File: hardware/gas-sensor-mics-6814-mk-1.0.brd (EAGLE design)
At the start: 25.4 x 22.9 mm, 7 parts, among them U1 MICS-6814

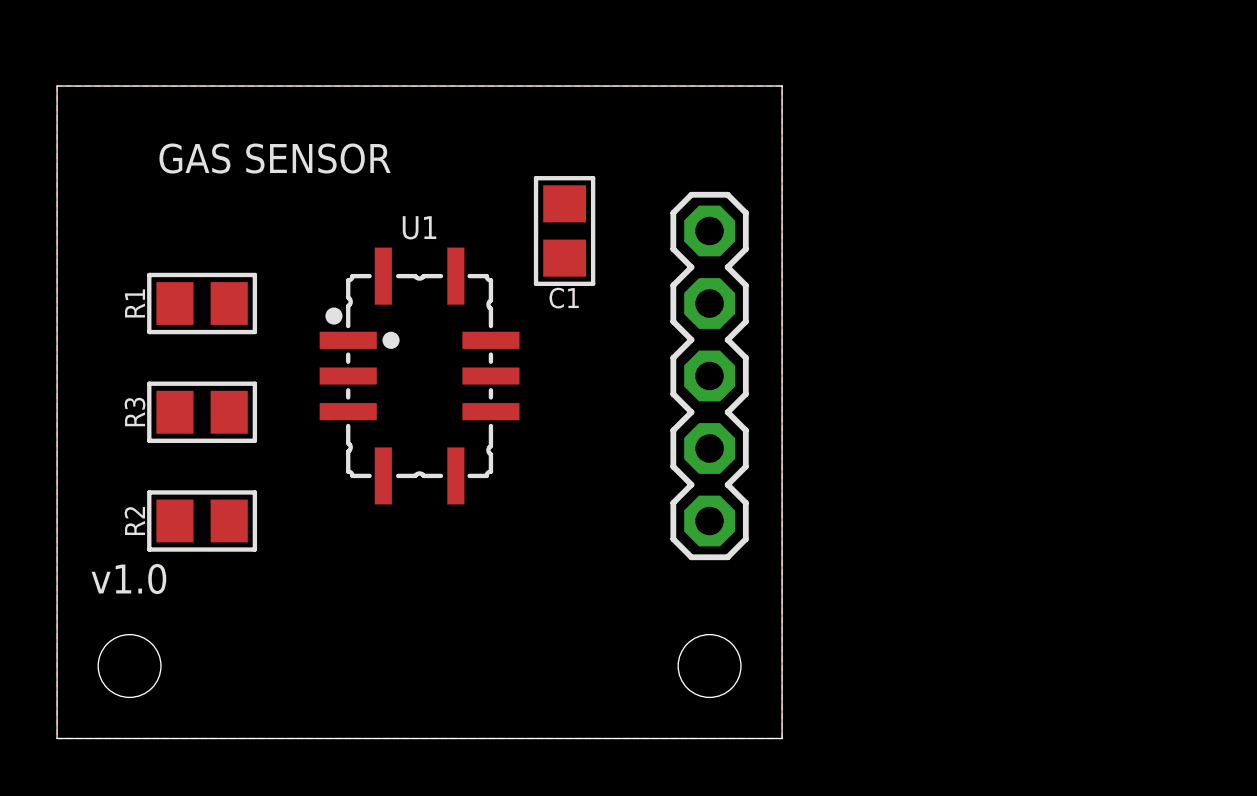
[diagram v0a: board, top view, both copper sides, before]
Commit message: gas sensor test boards
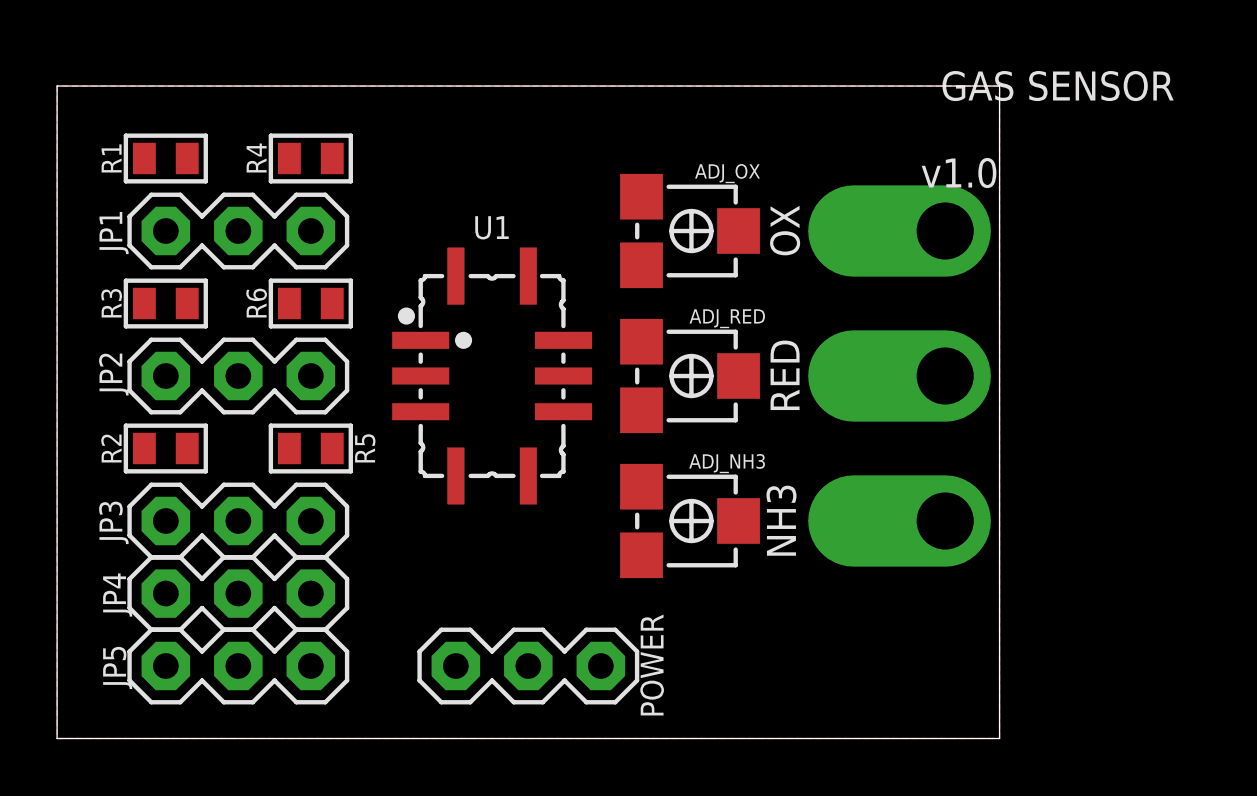
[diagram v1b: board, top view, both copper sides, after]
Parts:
- removed C1: 10u, a_parts:C0805
- added ADJ_NH3, ADJ_OX, ADJ_RED: (no value), a_parts:EVM3Y
- added JP2, JP3, JP4, JP5, POWER: M03PTH-CENTERED, a_parts:1X03-CENTERED
- added NH3, OX, RED: M01PTH-2MM-OFFSET, a_parts:1X01_2MM_OFFSET
- added R4: 75R, a_parts:R0603-TIGHTER
- added R5: 510R, a_parts:R0603-TIGHTER
- added R6: 10R, a_parts:R0603-TIGHTER
- JP1: value M05PTH-CENTERED -> M03PTH-CENTERED; device a_parts:1X05_PTH_CENTERED -> a_parts:1X03-CENTERED
- R1, R2, R3: device a_parts:R0805 -> a_parts:R0603-TIGHTER
- moved JP1 17.3 mm to (6.35, 17.8), turned to 0 degrees
- moved R1 5.24 mm to (3.81, 20.3)
- moved R3 4.02 mm to (3.81, 15.2)
- moved R2 2.84 mm to (3.81, 10.2)
- moved U1 2.54 mm to (15.2, 12.7)
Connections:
- removed net N$4: R2.2, U1.E, U1.G
- removed net VCC: C1.1, JP1.2, R1.1, R2.1, R3.1
- new net 3.3V: POWER.2, R4.1, R5.1, R6.2
- new net 5V: POWER.3, R1.1, R2.1, R3.1
- new net N$11: JP3.3, JP5.3, R5.2
- new net N$12: JP3.1, JP5.1, R2.2
- new net N$13: JP4.1, JP5.2
- new net N$2: ADJ_NH3.S, NH3.1
- new net N$3: ADJ_RED.S, RED.1
- new net N$5: ADJ_OX.S, OX.1
- new net N$7: JP1.3, R4.2
- new net N$8: JP2.3, R6.1
- new net NH3_HEAT1_IN: JP2.2, U1.C
- new net NH3_HEAT2_IN: JP4.2, U1.E
- new net OX_HEAT2_IN: JP1.2, U1.K
- new net RED_HEAT2_IN: JP3.2, U1.G
- net GND: now also ADJ_NH3.E, ADJ_OX.E, ADJ_RED.E, POWER.1; no longer C1.2, JP1.1
- net N$1: now also JP2.1; no longer U1.C
- net N$6: now also JP1.1; no longer U1.K
- net NH3_OUT: now also ADJ_NH3.A; no longer JP1.5
- net OX_OUT: now also ADJ_OX.A; no longer JP1.4
- net RED_OUT: now also ADJ_RED.A; no longer JP1.3
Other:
- board size 25.4 x 22.9 mm -> 33 x 22.9 mm
